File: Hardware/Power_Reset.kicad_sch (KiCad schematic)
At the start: 49 parts, among them IC18 74HC139, IC27 74HC32, IC28 74HC00, IC29 74AHC04, IC30 74HC02, IC54 74HC123, J107 Power In, Q101 BC548, SW101 Reset, SW102 Power, U101 74AHCU04, U102 LM7805CT, U103 LM7812CT

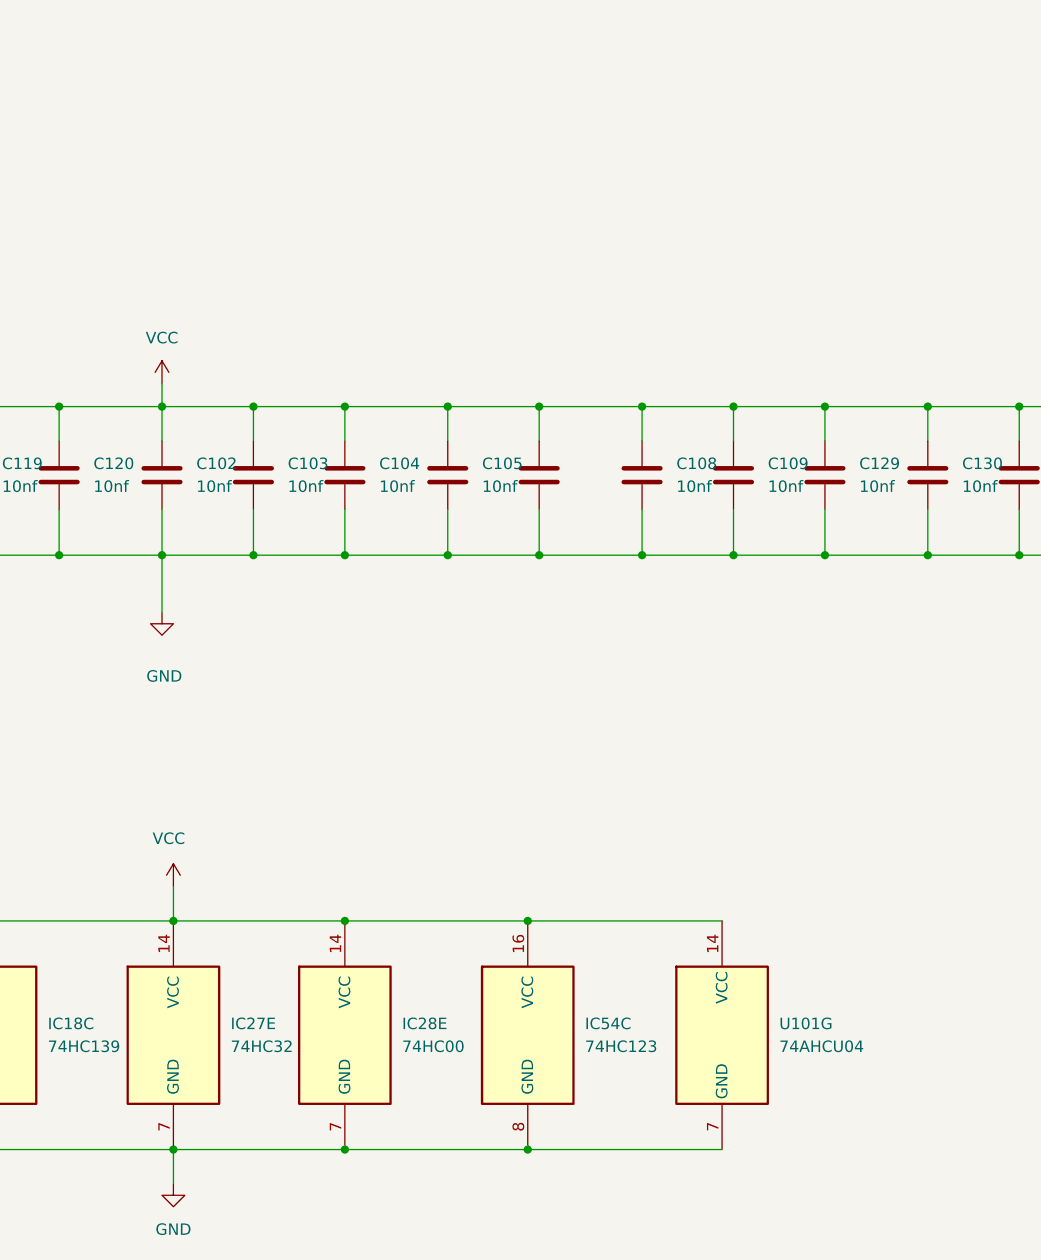
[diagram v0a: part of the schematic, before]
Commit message: Fixed some issues with memory mapping IC 25
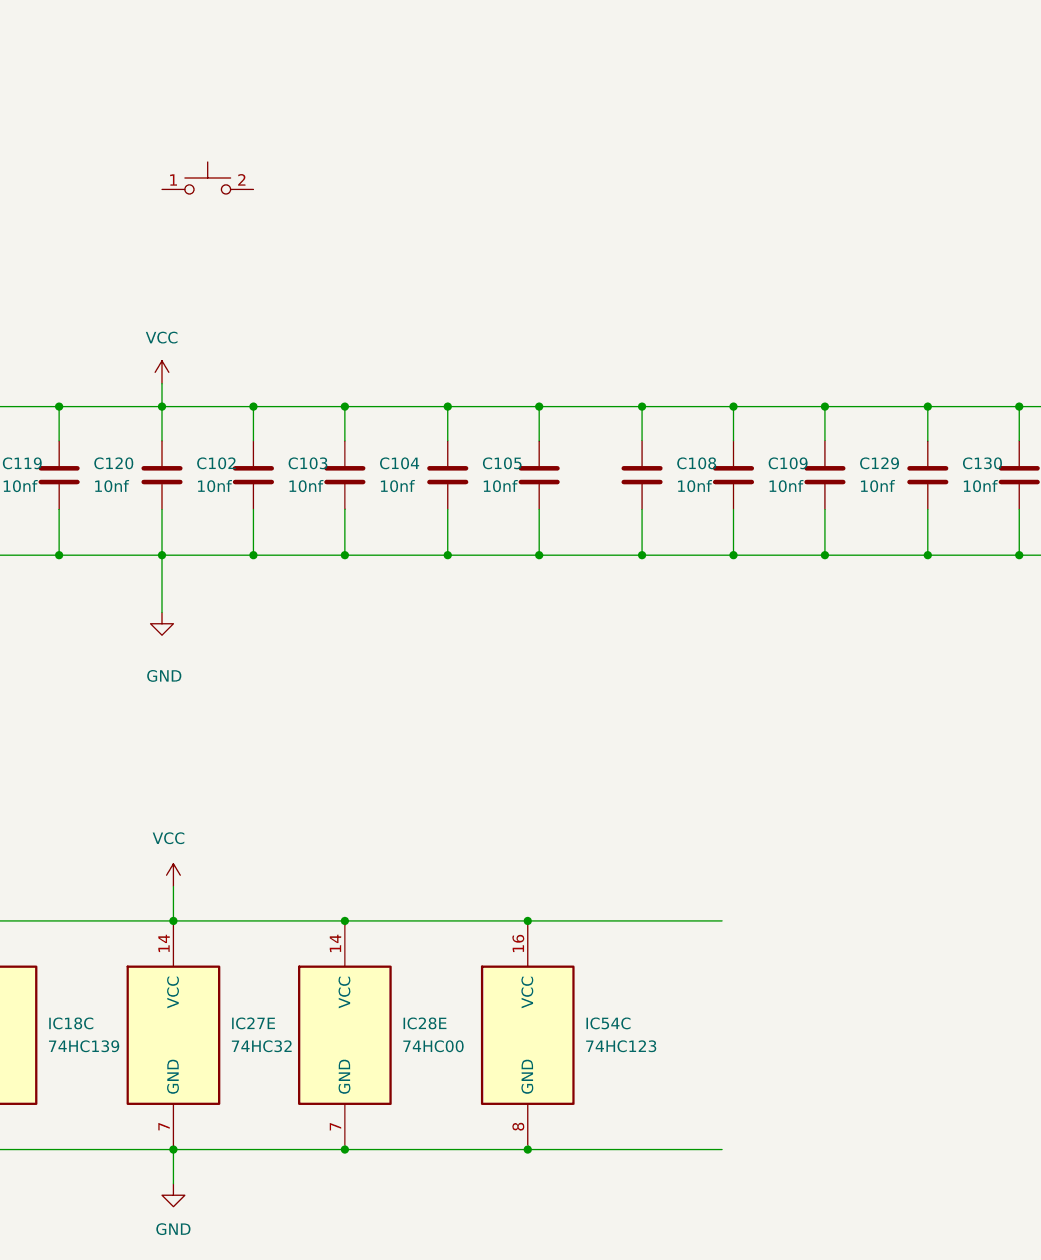
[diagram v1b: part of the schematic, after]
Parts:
- removed unit 7 of U101
- added SW1: Push_button, artemisa:Push_button_angled, symbol artemisa:Push_button
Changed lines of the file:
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@@
 	)
 	(symbol
-		(lib_id "74xx:74LS04")
-		(at 261.62 222.25 0)
-		(unit 7)
+		(lib_id "artemisa:Push_button")
+		(at 204.47 128.27 0)
+		(unit 1)
 		(exclude_from_sim no)
 		(in_bom yes)
 		(on_board yes)
 		(dnp no)
-		(fields_autoplaced yes)
-		(property "Reference" "U101"
-			(at 267.97 220.9799 0)
-			(effects
-				(font
-					(size 1.27 1.27)
-				)
-				(justify left)
-			)
-		)
-		(property "Value" "74AHCU04"
-			(at 267.97 223.5199 0)
-			(effects
-				(font
-					(size 1.27 1.27)
-				)
-				(justify left)
-			)
-		)
-		(property "Footprint" "Package_DIP:DIP-14_W7.62mm_Socket_LongPads"
-			(at 261.62 222.25 0)
+		(property "Reference" "SW1"
+			(at 204.47 123.1646 0)
 			(effects
 				(font
@@
 			)
 		)
-		(property "Datasheet" "http://www.ti.com/lit/gpn/sn74LS04"
-			(at 261.62 222.25 0)
+		(property "Value" "Push_button"
+			(at 204.47 130.81 0)
+			(effects
+				(font
+					(size 1.524 1.524)
+				)
+				(hide yes)
+			)
+		)
+		(property "Footprint" "artemisa:Push_button_angled"
+			(at 204.47 128.27 0)
+			(effects
+				(font
+					(size 1.524 1.524)
+				)
+				(hide yes)
+			)
+		)
+		(property "Datasheet" ""
+			(at 204.47 128.27 0)
+			(effects
+				(font
+					(size 1.524 1.524)
+				)
+				(hide yes)
+			)
+		)
+		(property "Description" ""
+			(at 204.47 128.27 0)
 			(effects
 				(font
@@
 			)
 		)
-		(property "Description" "Hex Inverter"
-			(at 261.62 222.25 0)
-			(effects
-				(font
-					(size 1.27 1.27)
-				)
-				(hide yes)
-			)
-		)
-		(pin "6"
-		)
 		(pin "1"
-		)
-		(pin "14"
-		)
-		(pin "10"
-		)
-		(pin "12"
-		)
-		(pin "11"
-		)
-		(pin "13"
-		)
-		(pin "4"
-		)
-		(pin "9"
-		)
-		(pin "5"
-		)
-		(pin "8"
-		)
-		(pin "7"
-		)
-		(pin "3"
 		)
 		(pin "2"
@@
 			(project "CPU_Board"
 				(path "/f5b991b2-bbcb-4d6c-a89c-6801c3d50251/b1de1a07-b966-4887-998c-65d3c92f37fe"
-					(reference "U101")
-					(unit 7)
+					(reference "SW1")
+					(unit 1)
 				)
 			)
